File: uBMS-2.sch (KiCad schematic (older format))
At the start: 65 parts

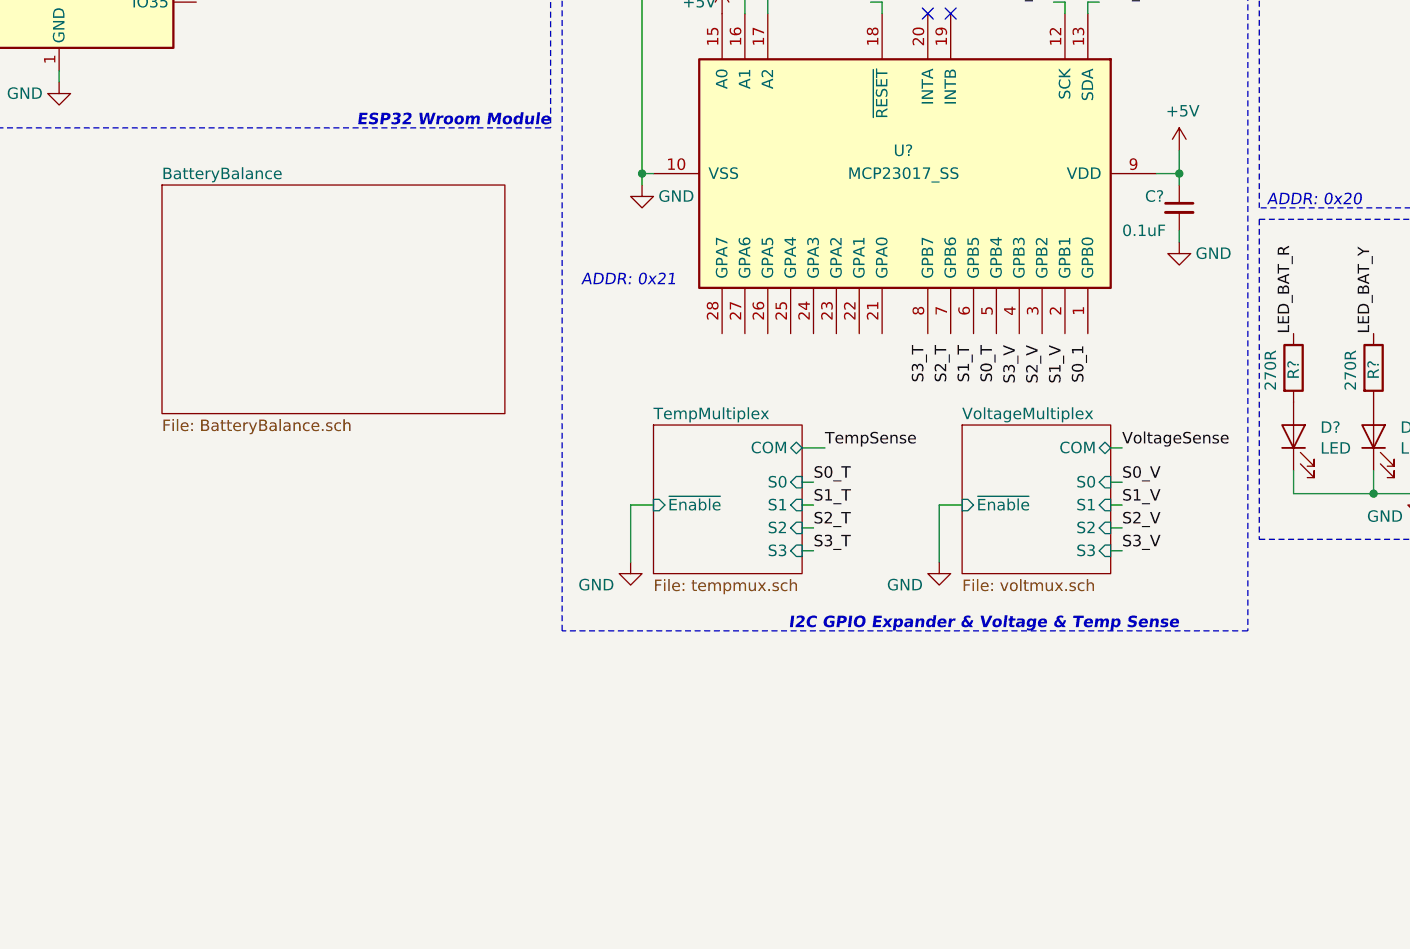
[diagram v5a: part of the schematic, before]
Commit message: Connected Balance Sheet
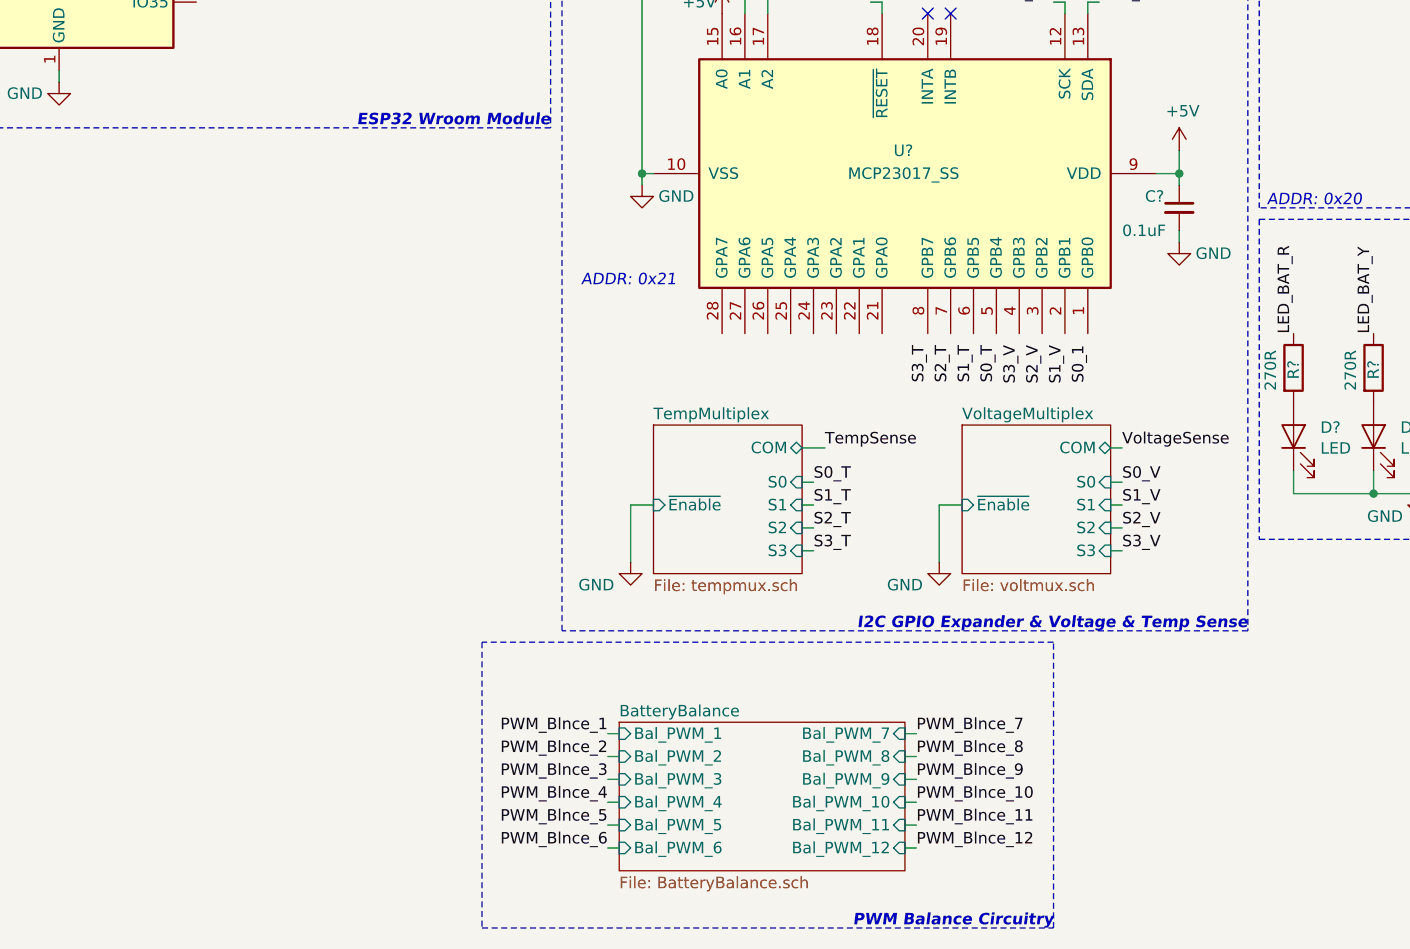
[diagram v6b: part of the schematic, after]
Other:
- note added: "PWM Balance Circuitry"
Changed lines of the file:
@@
 Wire Wire Line
 	7050 3700 7100 3700
-Text Notes 7450 6450 2    50   Italic 10
+Text Notes 7750 6450 2    50   Italic 10
 I2C GPIO Expander & Voltage & Temp Sense
 $Sheet
-S 3000 4500 1500 1000
+S 5000 6850 1250 650
 U 5F7870B7
 F0 "BatteryBalance" 50
 F1 "BatteryBalance.sch" 50
+F2 "Bal_PWM_1" I L 5000 6900 50
+F3 "Bal_PWM_2" I L 5000 7000 50
+F4 "Bal_PWM_3" I L 5000 7100 50
+F5 "Bal_PWM_4" I L 5000 7200 50
+F6 "Bal_PWM_5" I L 5000 7300 50
+F7 "Bal_PWM_6" I L 5000 7400 50
+F8 "Bal_PWM_7" I R 6250 6900 50
+F9 "Bal_PWM_8" I R 6250 7000 50
+F10 "Bal_PWM_9" I R 6250 7100 50
+F11 "Bal_PWM_10" I R 6250 7200 50
+F12 "Bal_PWM_11" I R 6250 7300 50
+F13 "Bal_PWM_12" I R 6250 7400 50
 $EndSheet
+Text Label 4950 6900 2    50   ~ 0
+PWM_Blnce_1
+Text Label 4950 7000 2    50   ~ 0
+PWM_Blnce_2
+Text Label 4950 7100 2    50   ~ 0
+PWM_Blnce_3
+Text Label 4950 7200 2    50   ~ 0
+PWM_Blnce_4
+Text Label 4950 7300 2    50   ~ 0
+PWM_Blnce_5
+Text Label 4950 7400 2    50   ~ 0
+PWM_Blnce_6
+Text Label 6300 6900 0    50   ~ 0
+PWM_Blnce_7
+Text Label 6300 7000 0    50   ~ 0
+PWM_Blnce_8
+Text Label 6300 7100 0    50   ~ 0
+PWM_Blnce_9
+Text Label 6300 7200 0    50   ~ 0
+PWM_Blnce_10
+Text Label 6300 7300 0    50   ~ 0
+PWM_Blnce_11
+Text Label 6300 7400 0    50   ~ 0
+PWM_Blnce_12
+Wire Wire Line
+	4950 6900 5000 6900
+Wire Wire Line
+	4950 7000 5000 7000
+Wire Wire Line
+	4950 7100 5000 7100
+Wire Wire Line
+	4950 7200 5000 7200
+Wire Wire Line
+	4950 7300 5000 7300
+Wire Wire Line
+	4950 7400 5000 7400
+Wire Wire Line
+	6300 6900 6250 6900
+Wire Wire Line
+	6300 7000 6250 7000
+Wire Wire Line
+	6300 7100 6250 7100
+Wire Wire Line
+	6300 7200 6250 7200
+Wire Wire Line
+	6300 7300 6250 7300
+Wire Wire Line
+	6300 7400 6250 7400
+Wire Notes Line
+	6900 6500 4400 6500
+Wire Notes Line
+	4400 6500 4400 7750
+Wire Notes Line
+	4400 7750 6900 7750
+Wire Notes Line
+	6900 7750 6900 6500
+Text Notes 6900 7750 2    50   Italic 10
+PWM Balance Circuitry
 $EndSCHEMATC

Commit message: Think I just added labels?
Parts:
- gave numbers to parts that had none: 63
- renumbered CIN to CIN1, COUT to COUT1
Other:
- note added: "Tie reset to GPIO expander too\nMight have to add Diode and 5v pullup\n\n"
- note removed: "Tie reset to GPIO expander too\n"
- moved on the sheet: C5, C6, U2

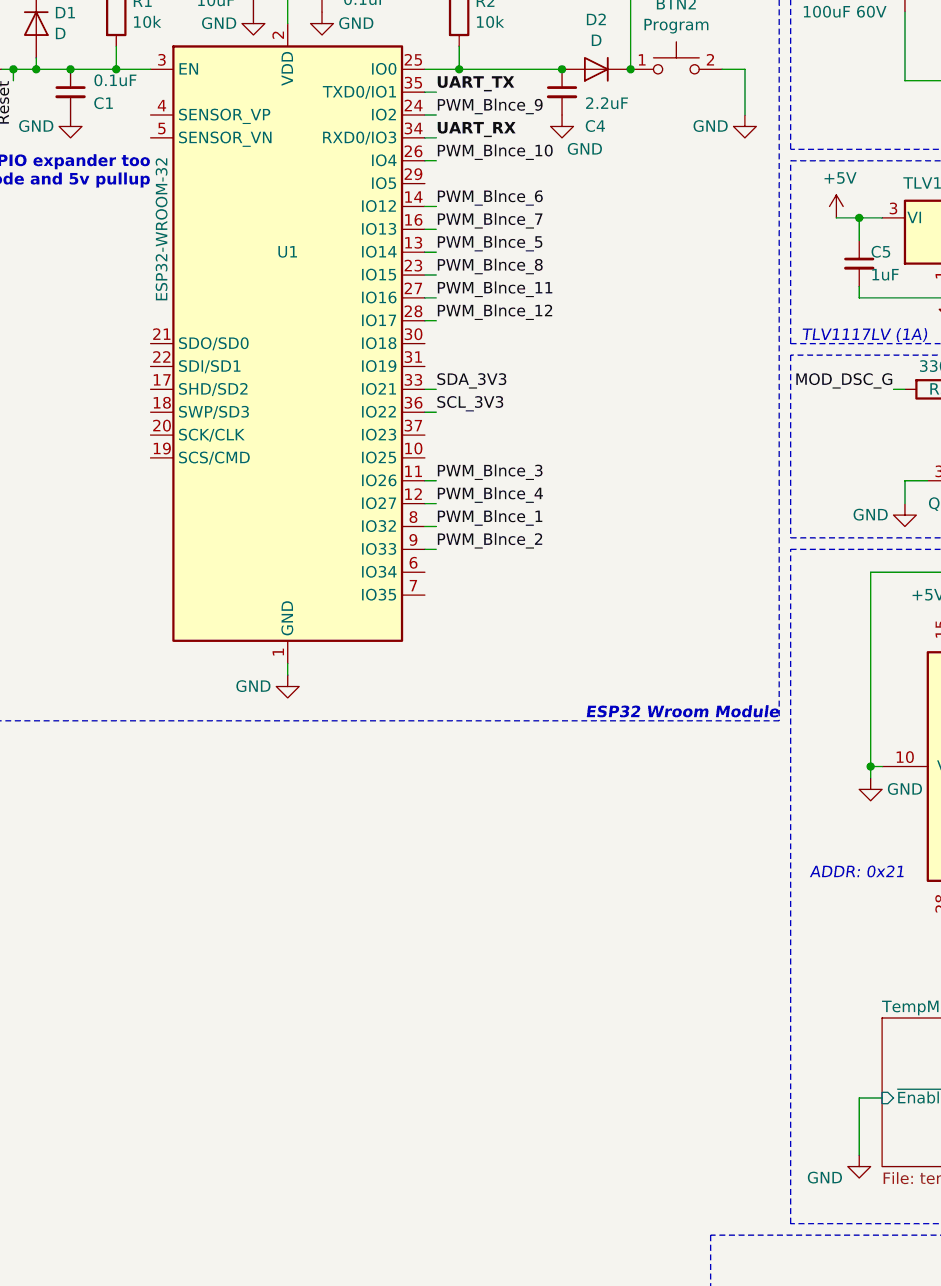
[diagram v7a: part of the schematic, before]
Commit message: Added Micro SD Card Interface
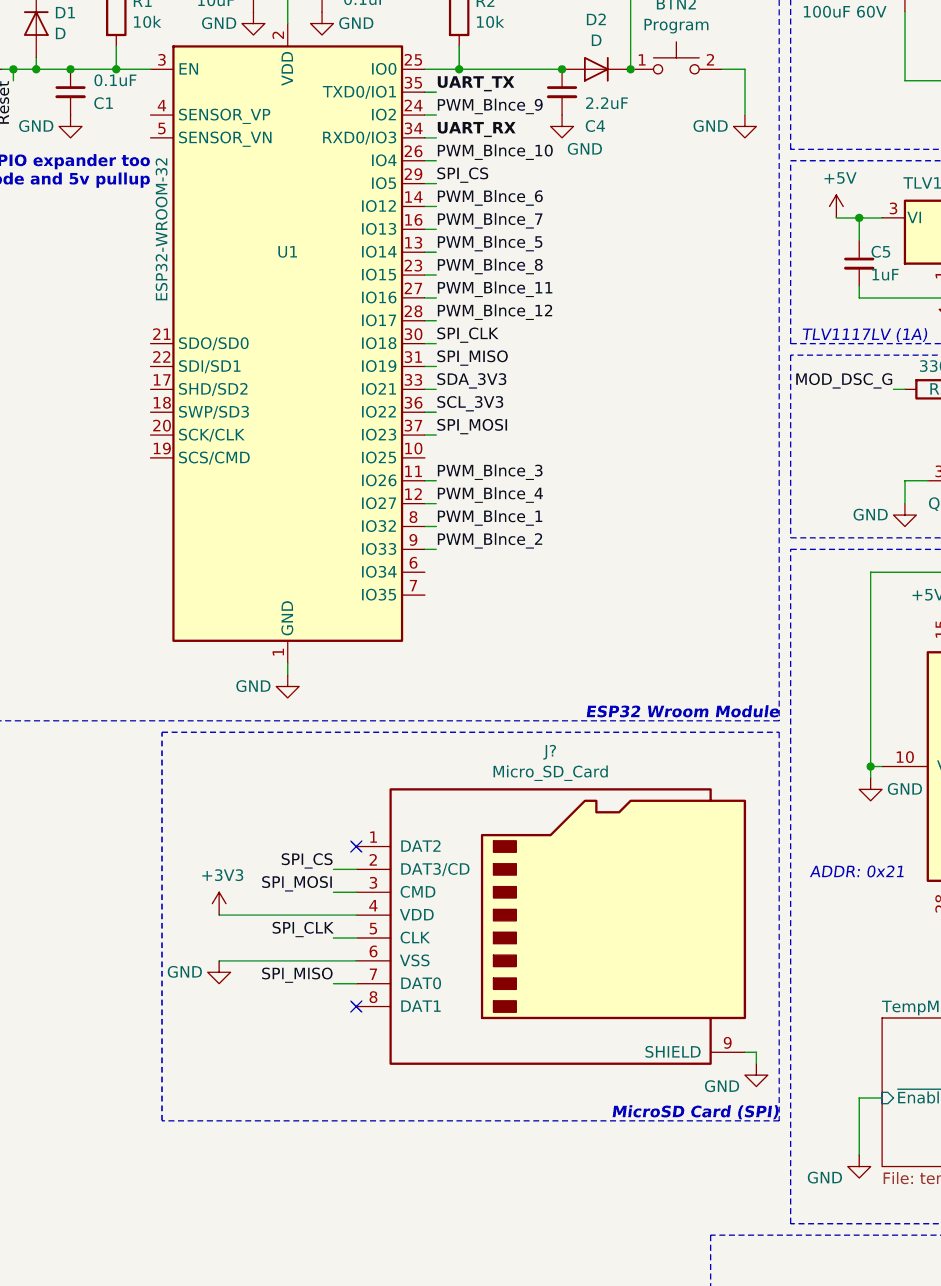
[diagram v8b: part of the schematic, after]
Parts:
- added J?: Micro_SD_Card, symbol Connector:Micro_SD_Card
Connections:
- net +3V3: now also J?.4 (VDD)
- net GND: now also J?.6 (VSS), J?.9 (SHIELD)
- net SPI_CS: now reaches U1.29 (IO5)
- net SPI_CS: now also J?.2 (DAT3/CD)
- net SPI_CLK: now reaches U1.30 (IO18)
- net SPI_CLK: now also J?.5 (CLK)
- net SPI_MISO: now reaches U1.31 (IO19)
- net SPI_MISO: now also J?.7 (DAT0)
- net SPI_MOSI: now reaches U1.37 (IO23)
- net SPI_MOSI: now also J?.3 (CMD)
- no-connect marks 2 -> 4
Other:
- note added: "MicroSD Card (SPI)"
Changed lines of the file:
@@
 Wire Notes Line
 	4750 2600 6150 2600
+$Comp
+L Connector:Micro_SD_Card J?
+U 1 1 5F239FEE
+P 3750 5100
+F 0 "J?" H 3700 5817 50  0000 C CNN
+F 1 "Micro_SD_Card" H 3700 5726 50  0000 C CNN
+F 2 "" H 4900 5400 50  0001 C CNN
+F 3 "http://katalog.we-online.de/em/datasheet/693072010801.pdf" H 3750 5100 50  0001 C CNN
+	1    3750 5100
+	1    0    0    -1
+$EndComp
+$Comp
+L power:GND #PWR?
+U 1 1 5F23C6D3
+P 4600 5750
+F 0 "#PWR?" H 4600 5500 50  0001 C CNN
+F 1 "GND" H 4450 5650 50  0000 C CNN
+F 2 "" H 4600 5750 50  0001 C CNN
+F 3 "" H 4600 5750 50  0001 C CNN
+	1    4600 5750
+	1    0    0    -1
+$EndComp
+Wire Wire Line
+	4600 5750 4600 5700
+Wire Wire Line
+	4600 5700 4550 5700
+Text Label 3200 1900 0    50   ~ 0
+SPI_CS
+Text Label 3200 3000 0    50   ~ 0
+SPI_MOSI
+Text Label 3200 2600 0    50   ~ 0
+SPI_CLK
+Text Label 3200 2700 0    50   ~ 0
+SPI_MISO
+Wire Wire Line
+	3200 1900 3150 1900
+Wire Wire Line
+	3200 2600 3150 2600
+Wire Wire Line
+	3200 2700 3150 2700
+Wire Wire Line
+	3200 3000 3150 3000
+Text Label 2750 4900 2    50   ~ 0
+SPI_CS
+Text Label 2750 5000 2    50   ~ 0
+SPI_MOSI
+Text Label 2750 5200 2    50   ~ 0
+SPI_CLK
+Text Label 2750 5400 2    50   ~ 0
+SPI_MISO
+Wire Wire Line
+	2750 5400 2850 5400
+Wire Wire Line
+	2750 5200 2850 5200
+Wire Wire Line
+	2750 5000 2850 5000
+Wire Wire Line
+	2750 4900 2850 4900
+$Comp
+L power:+3V3 #PWR?
+U 1 1 5F3038DF
+P 2250 5100
+F 0 "#PWR?" H 2250 4950 50  0001 C CNN
+F 1 "+3V3" H 2265 5273 50  0000 C CNN
+F 2 "" H 2250 5100 50  0001 C CNN
+F 3 "" H 2250 5100 50  0001 C CNN
+	1    2250 5100
+	1    0    0    -1
+$EndComp
+Wire Wire Line
+	2250 5100 2850 5100
+$Comp
+L power:GND #PWR?
+U 1 1 5F31AA65
+P 2250 5300
+F 0 "#PWR?" H 2250 5050 50  0001 C CNN
+F 1 "GND" H 2100 5250 50  0000 C CNN
+F 2 "" H 2250 5300 50  0001 C CNN
+F 3 "" H 2250 5300 50  0001 C CNN
+	1    2250 5300
+	1    0    0    -1
+$EndComp
+Wire Wire Line
+	2250 5300 2850 5300
+NoConn ~ 2850 5500
+NoConn ~ 2850 4800
+Wire Notes Line
+	4700 4300 4700 6000
+Wire Notes Line
+	4700 6000 2000 6000
+Wire Notes Line
+	2000 6000 2000 4300
+Wire Notes Line
+	2000 4300 4700 4300
+Text Notes 4700 6000 2    50   Italic 10
+MicroSD Card (SPI)
 $EndSCHEMATC
